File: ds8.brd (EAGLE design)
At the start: 85 x 50 mm, 92 parts, among them IC1 TM4C1230C3PM, IC2 TPS77333, Q1 BC850, Q2 BC850, Q3 BC850, U1 LM13700M, U2 LM324, U3 LM324, U4 LM741D, X1 MAB5SH

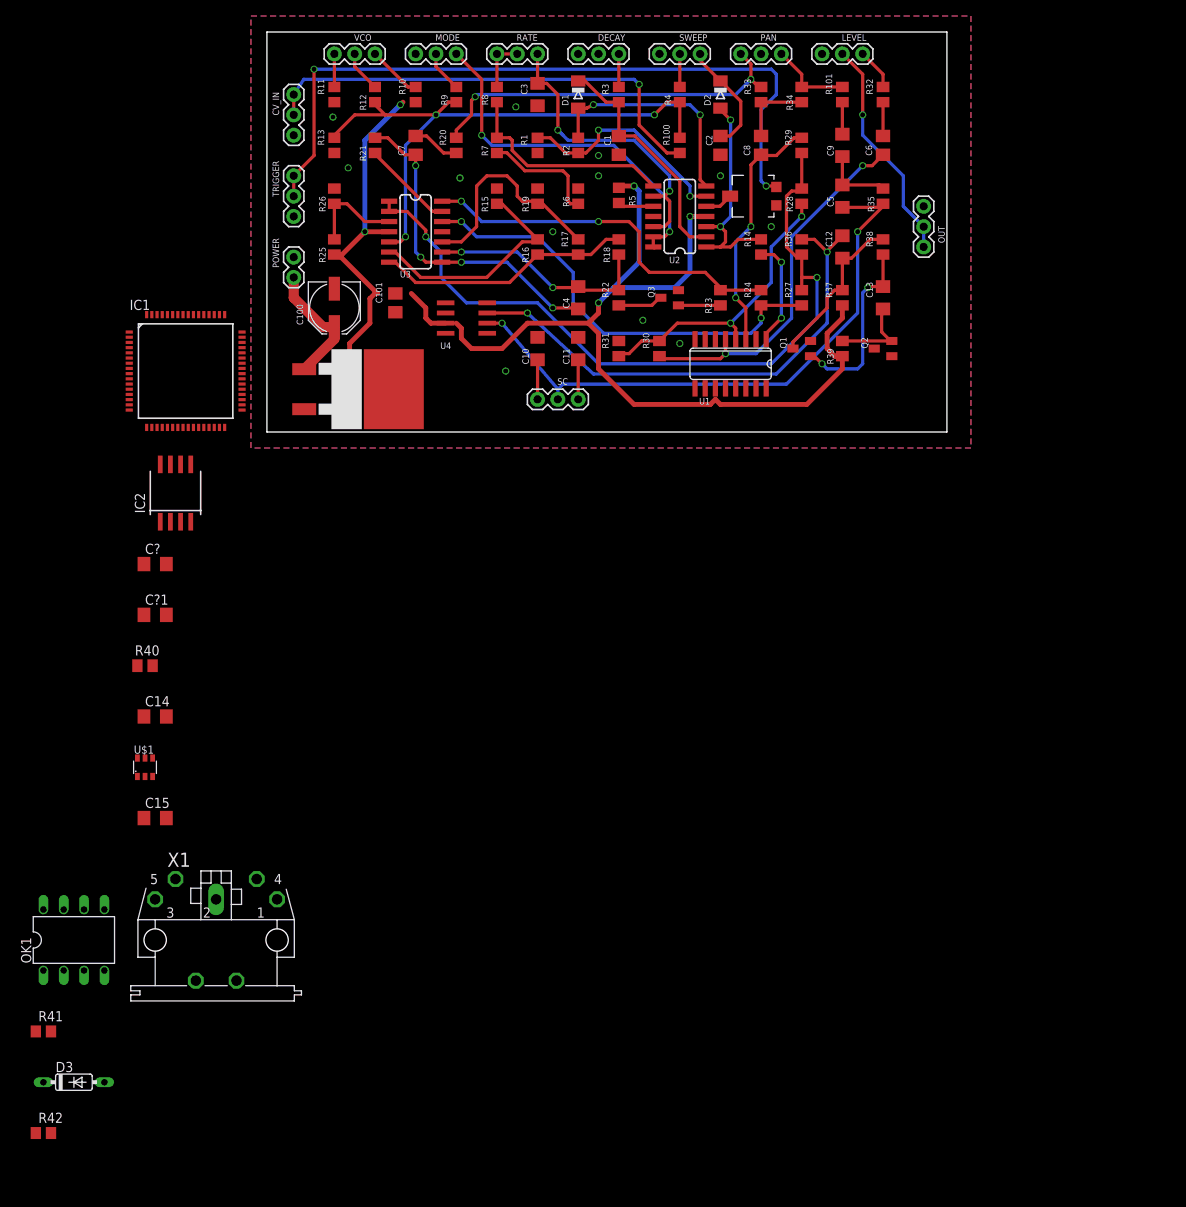
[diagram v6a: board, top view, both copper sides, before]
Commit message: added midi trigger
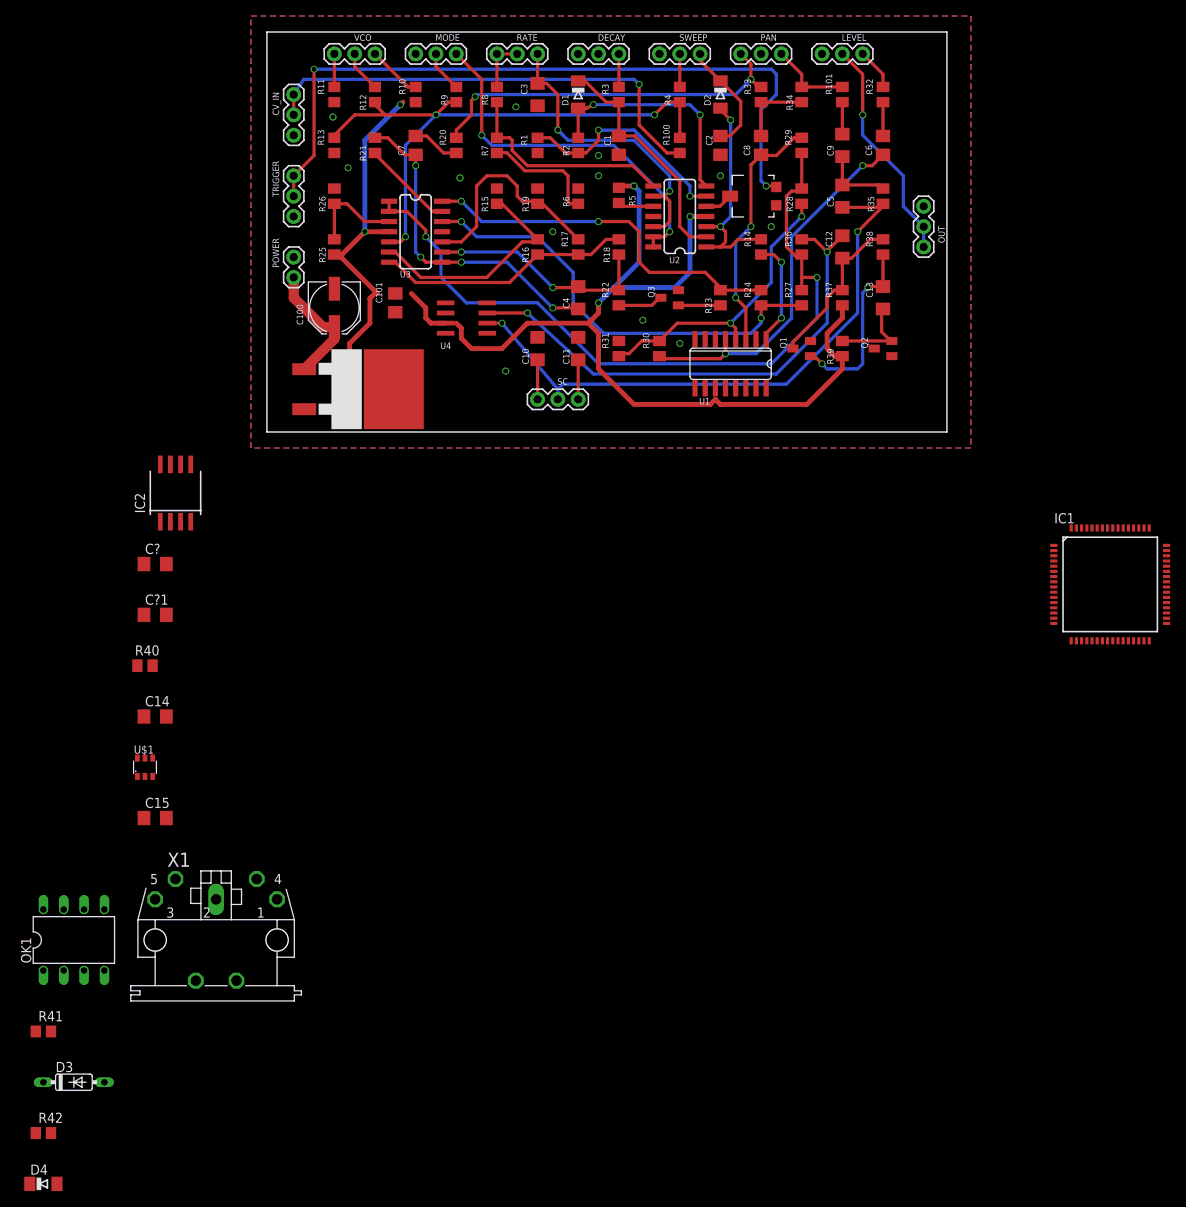
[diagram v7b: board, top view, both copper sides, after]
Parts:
- added D4: 4148, diode:MINIMELF
- moved IC1 118.6 mm to (105.4, -19.1)
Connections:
- new net MIDI_TRIG: D4.A, IC1.61
- net N$3: now also D4.C
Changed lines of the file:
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@@
 <attribute name="VALUE" x="36.37" y="1.54" size="0.6096" layer="27"/>
 </element>
-<element name="IC1" library="TM4" package="LQFP_64" value="TM4C1230C3PM" x="-10.16" y="7.62"/>
+<element name="IC1" library="TM4" package="LQFP_64" value="TM4C1230C3PM" x="105.41" y="-19.05"/>
 <element name="IC2" library="texas" package="SOP-08" value="TPS77333" x="-11.43" y="-7.62">
 <attribute name="OC_NEWARK" value="02M1919" x="-11.43" y="-7.62" size="1.778" layer="27" display="off"/>
@@
 <element name="D3" library="diode" package="DO35-7" value="1N4148DO35-7" x="-24.13" y="-81.28"/>
 <element name="R42" library="rcl" package="R0805" value="220" x="-27.94" y="-87.63"/>
+<element name="D4" library="diode" package="MINIMELF" value="4148" x="-27.94" y="-93.98"/>
 </elements>
 <signals>
@@
 <wire x1="54.9247" y1="24.4" x2="52.88" y2="24.4" width="0.4064" layer="1"/>
 <wire x1="52.88" y1="24.4" x2="51.61" y2="25.67" width="0.4064" layer="1"/>
+<contactref element="D4" pad="C"/>
+<wire x1="52.88" y1="24.4" x2="-29.64" y2="-93.98" width="0" layer="19" extent="1-1"/>
 </signal>
 <signal name="N$4">
@@
 <wire x1="67.95" y1="11.38" x2="56.055" y2="11.5984" width="0" layer="19" extent="1-1"/>
 <wire x1="78.11" y1="9.48" x2="67.95" y2="11.38" width="0" layer="19" extent="1-1"/>
-<wire x1="-9.185" y1="14.67" x2="3.35" y2="21.86" width="0" layer="19" extent="1-1"/>
-<wire x1="-17.21" y1="11.195" x2="-9.185" y2="14.67" width="0" layer="19" extent="1-1"/>
-<wire x1="-17.21" y1="5.345" x2="-17.21" y2="11.195" width="0" layer="19" extent="1-1"/>
-<wire x1="-8.535" y1="0.57" x2="-17.21" y2="5.345" width="0" layer="19" extent="1-1"/>
-<wire x1="-3.11" y1="6.645" x2="-8.535" y2="0.57" width="0" layer="19" extent="1-1"/>
-<wire x1="-9.525" y1="-11.22" x2="-8.535" y2="0.57" width="0" layer="19" extent="1-1"/>
+<wire x1="106.385" y1="-12" x2="3.35" y2="21.86" width="0" layer="19" extent="1-1"/>
+<wire x1="98.36" y1="-15.475" x2="106.385" y2="-12" width="0" layer="19" extent="1-1"/>
+<wire x1="98.36" y1="-21.325" x2="98.36" y2="-15.475" width="0" layer="19" extent="1-1"/>
+<wire x1="107.035" y1="-26.1" x2="98.36" y2="-21.325" width="0" layer="19" extent="1-1"/>
+<wire x1="112.46" y1="-20.025" x2="107.035" y2="-26.1" width="0" layer="19" extent="1-1"/>
+<wire x1="-9.525" y1="-11.22" x2="107.035" y2="-26.1" width="0" layer="19" extent="1-1"/>
 <wire x1="-10.795" y1="-11.22" x2="-9.525" y2="-11.22" width="0" layer="19" extent="1-1"/>
 <wire x1="-15.37" y1="-16.51" x2="-10.795" y2="-11.22" width="0" layer="19" extent="1-1"/>
@@
 <wire x1="-13.335" y1="-4.045" x2="-13.335" y2="-11.22" width="0" layer="19" extent="1-1"/>
 <wire x1="-12.065" y1="-4.045" x2="-13.335" y2="-4.045" width="0" layer="19" extent="1-1"/>
-<wire x1="-9.185" y1="0.57" x2="-12.065" y2="-4.045" width="0" layer="19" extent="1-1"/>
-<wire x1="-17.21" y1="5.995" x2="-9.185" y2="0.57" width="0" layer="19" extent="1-1"/>
-<wire x1="-17.21" y1="11.845" x2="-17.21" y2="5.995" width="0" layer="19" extent="1-1"/>
-<wire x1="-8.535" y1="14.67" x2="-17.21" y2="11.845" width="0" layer="19" extent="1-1"/>
-<wire x1="-3.11" y1="8.595" x2="-8.535" y2="14.67" width="0" layer="19" extent="1-1"/>
+<wire x1="106.385" y1="-26.1" x2="-12.065" y2="-4.045" width="0" layer="19" extent="1-1"/>
+<wire x1="98.36" y1="-20.675" x2="106.385" y2="-26.1" width="0" layer="19" extent="1-1"/>
+<wire x1="98.36" y1="-14.825" x2="98.36" y2="-20.675" width="0" layer="19" extent="1-1"/>
+<wire x1="107.035" y1="-12" x2="98.36" y2="-14.825" width="0" layer="19" extent="1-1"/>
+<wire x1="112.46" y1="-18.075" x2="107.035" y2="-12" width="0" layer="19" extent="1-1"/>
 </signal>
 <signal name="N$6">
 <contactref element="IC1" pad="25"/>
 <contactref element="C14" pad="2"/>
-<wire x1="-9.835" y1="0.57" x2="-12.57" y2="-35.56" width="0" layer="19" extent="1-1"/>
+<wire x1="105.735" y1="-26.1" x2="-12.57" y2="-35.56" width="0" layer="19" extent="1-1"/>
 </signal>
 <signal name="ARM_SSI0_FS">
@@
 <contactref element="U$1" pad="5"/>
 <wire x1="-15.24" y1="-40.76" x2="-16.19" y2="-40.76" width="0" layer="19" extent="1-1"/>
-<wire x1="-13.085" y1="0.57" x2="-15.24" y2="-40.76" width="0" layer="19" extent="1-1"/>
+<wire x1="102.485" y1="-26.1" x2="-15.24" y2="-40.76" width="0" layer="19" extent="1-1"/>
 </signal>
 <signal name="ARM_SSI0_CLK">
@@
 <contactref element="IC1" pad="22"/>
 <contactref element="U$1" pad="4"/>
-<wire x1="-11.785" y1="0.57" x2="-14.29" y2="-40.76" width="0" layer="19" extent="1-1"/>
+<wire x1="103.785" y1="-26.1" x2="-14.29" y2="-40.76" width="0" layer="19" extent="1-1"/>
 </signal>
 <signal name="/RESET">
@@
 <contactref element="IC1" pad="38"/>
 <wire x1="-12.065" y1="-11.22" x2="-14.29" y2="-29.21" width="0" layer="19" extent="1-1"/>
-<wire x1="-3.11" y1="5.995" x2="-12.065" y2="-11.22" width="0" layer="19" extent="1-1"/>
+<wire x1="112.46" y1="-20.675" x2="-12.065" y2="-11.22" width="0" layer="19" extent="1-1"/>
 </signal>
 <signal name="N$36">
 <contactref element="C15" pad="2"/>
 <contactref element="IC1" pad="56"/>
-<wire x1="-9.835" y1="14.67" x2="-12.57" y2="-48.26" width="0" layer="19" extent="1-1"/>
+<wire x1="105.735" y1="-12" x2="-12.57" y2="-48.26" width="0" layer="19" extent="1-1"/>
 </signal>
 <signal name="PE">
@@
 <contactref element="IC1" pad="17"/>
 <wire x1="-22.86" y1="-59.69" x2="-28.89" y2="-87.63" width="0" layer="19" extent="1-1"/>
-<wire x1="-15.035" y1="0.57" x2="-22.86" y2="-59.69" width="0" layer="19" extent="1-1"/>
+<wire x1="100.535" y1="-26.1" x2="-22.86" y2="-59.69" width="0" layer="19" extent="1-1"/>
 </signal>
 <signal name="SWCLK">
 <contactref element="IC1" pad="52"/>
 <contactref element="X1" pad="1"/>
-<wire x1="-7.235" y1="14.67" x2="1.27" y2="-58.42" width="0" layer="19" extent="1-1"/>
+<wire x1="108.335" y1="-12" x2="1.27" y2="-58.42" width="0" layer="19" extent="1-1"/>
 </signal>
 <signal name="SWDIO">
 <contactref element="IC1" pad="51"/>
 <contactref element="X1" pad="3"/>
-<wire x1="-6.585" y1="14.67" x2="-13.97" y2="-58.42" width="0" layer="19" extent="1-1"/>
+<wire x1="108.985" y1="-12" x2="-13.97" y2="-58.42" width="0" layer="19" extent="1-1"/>
+</signal>
+<signal name="MIDI_TRIG">
+<contactref element="IC1" pad="61"/>
+<contactref element="D4" pad="A"/>
+<wire x1="102.485" y1="-12" x2="-26.24" y2="-93.98" width="0" layer="19" extent="1-1"/>
 </signal>
 </signals>
